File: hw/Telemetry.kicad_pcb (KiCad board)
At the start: 4 copper layers, 100 x 82 mm, 132 parts, among them J102 BOOT0, J103 SPORT, J104 SBUS, J105 USB_B_Micro, J106 UART_EXP, J201 Conn_01x02, J301 Conn_01x02, J302 Conn_01x02, J401 Conn_01x02, J402 Conn_01x02, J403 Conn_01x02, J404 Conn_01x02, J405 Conn_01x02, J406 Conn_01x02, J407 Conn_01x02, J408 Conn_01x02, J409 ServoCon, J410 AUDIO, Q401 IRLML6344TRPBF, Q402 IRLML6344TRPBF, Q403 IRLML6344TRPBF, Q404 CSD17306Q5A, Q406 IRLML6344TRPBF, Q408 CSD17306Q5A, SW101 SW_Push, U101 STM32F303CBx, U102 IS25LP032D, U201 AP1501-K5, U202 RT6200, U301 LP2985-5.0, U302 ACS770xCB-100U-PSF, U303 MCP6001-OT, U304 ACS770xCB-100U-PSF, U305 MCP6001-OT, U401 MCP1416, U402 MCP1416, U403 AD5160BRJZ10-R2, U404 MCP6001-OT, U405 TLP2361_TPL_E, U406 TLP2361_TPL_E, X101 SG-310_SCF_8.000000MHZ

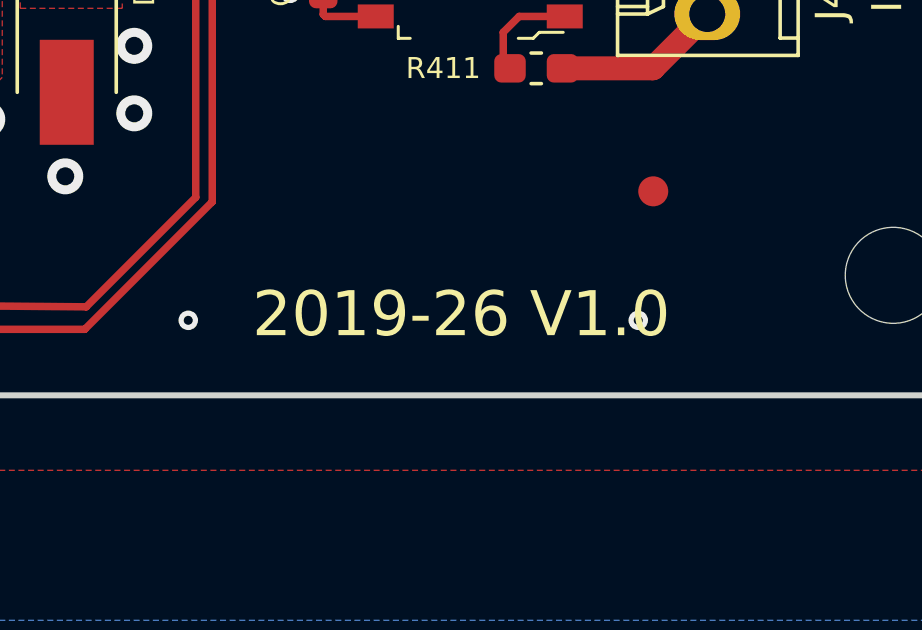
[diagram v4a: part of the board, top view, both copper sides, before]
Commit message: Added board 3D model picture to readme
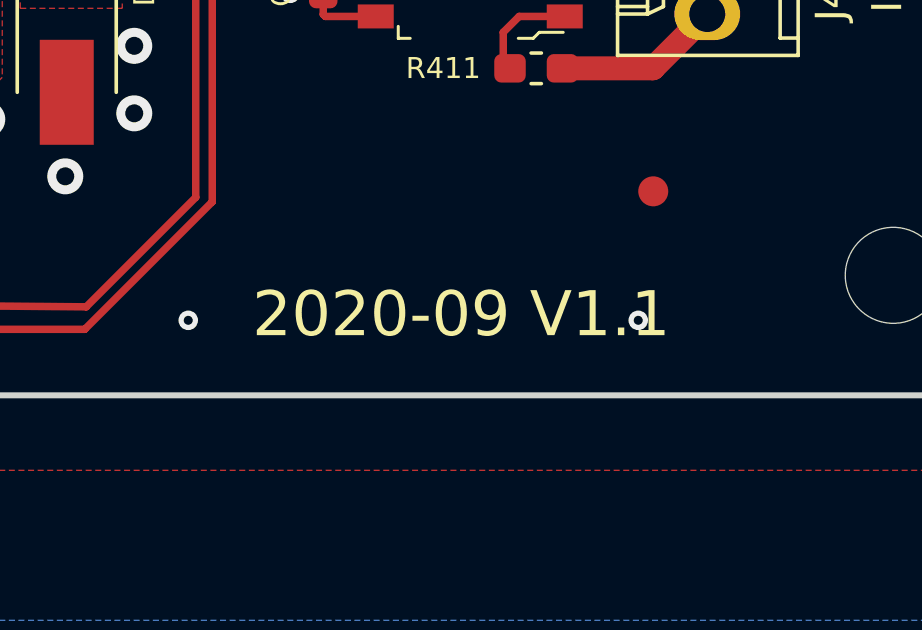
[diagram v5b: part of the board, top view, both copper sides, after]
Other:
- board text added: "2020-09 V1.1"
- board text removed: "2019-26 V1.0"
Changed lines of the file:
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@@
     (pad 1 smd rect (at -5.25 0) (size 4.5 5) (layers F.Cu F.Paste F.Mask)
       (net 9 "Net-(D202-Pad1)"))
+    (model ${KISYS3DMOD}/Inductor_SMD.3dshapes/L_Bourns_SRR1260.step
+      (at (xyz 0 0 0))
+      (scale (xyz 1 1 1))
+      (rotate (xyz 0 0 0))
+    )
   )
   (module digikey-footprints:SOT-23-3 (layer F.Cu)
@@
     (pad 6 smd rect (at -1.27 -3.15 90) (size 0.8 1.2) (layers F.Cu F.Paste F.Mask)
       (net 2 +3V3))
+    (model ${KISYS3DMOD}/Package_SO.3dshapes/SO-6_4.4x3.6mm_P1.27mm.step
+      (at (xyz 0 0 0))
+      (scale (xyz 1 1 1))
+      (rotate (xyz 0 0 -90))
+    )
   )
   (module digikey-footprints:SOIC-6-5_W4.55mm (layer F.Cu)
@@
     (pad 1 smd rect (at -1.27 3.15 90) (size 0.8 1.2) (layers F.Cu F.Paste F.Mask)
       (net 63 "Net-(R411-Pad1)"))
+    (model ${KISYS3DMOD}/Package_SO.3dshapes/SO-6_4.4x3.6mm_P1.27mm.step
+      (at (xyz 0 0 0))
+      (scale (xyz 1 1 1))
+      (rotate (xyz 0 0 -90))
+    )
   )
   (module Pin_Headers:Pin_Header_Straight_2x03 (layer F.Cu)
@@
     (pad 6 thru_hole oval (at 2.54 5.08) (size 1.7272 1.7272) (drill 1.016) (layers *.Cu *.Mask F.SilkS)
       (net 1 GND))
-    (model Pin_Headers.3dshapes/Pin_Header_Straight_2x03.wrl
-      (offset (xyz 1.269999980926514 -2.539999961853027 0))
+    (model ${KISYS3DMOD}/Connector_PinHeader_2.54mm.3dshapes/PinHeader_2x03_P2.54mm_Vertical.step
+      (at (xyz 0 0 0))
       (scale (xyz 1 1 1))
-      (rotate (xyz 0 0 90))
+      (rotate (xyz 0 0 0))
     )
   )
@@
     (pad 1 thru_hole rect (at 0 0 90) (size 1.7272 1.7272) (drill 1.016) (layers *.Cu *.Mask F.SilkS)
       (net 17 /Sbus))
-    (model Pin_Headers.3dshapes/Pin_Header_Straight_2x03.wrl
+    (model ${KISYS3DMOD}/Connector_PinHeader_2.54mm.3dshapes/PinHeader_2x03_P2.54mm_Vertical.step
       (offset (xyz 1.269999980926514 -2.539999961853027 0))
       (scale (xyz 1 1 1))
@@
     (pad 6 thru_hole oval (at 2.54 5.08 90) (size 1.7 1.7) (drill 1) (layers *.Cu *.Mask)
       (net 1 GND))
-    (model ${KISYS3DMOD}/Connector_PinHeader_2.54mm.3dshapes/PinHeader_2x03_P2.54mm_Vertical.wrl
+    (model ${KISYS3DMOD}/Connector_PinHeader_2.54mm.3dshapes/PinHeader_2x03_P2.54mm_Vertical.step
       (at (xyz 0 0 0))
       (scale (xyz 1 1 1))
@@
     (pad 4 thru_hole oval (at 2.54 2.54 90) (size 1.7 1.7) (drill 1) (layers *.Cu *.Mask)
       (net 1 GND))
-    (model ${KISYS3DMOD}/Connector_PinHeader_2.54mm.3dshapes/PinHeader_2x02_P2.54mm_Vertical.wrl
+    (model ${KISYS3DMOD}/Connector_PinHeader_2.54mm.3dshapes/PinHeader_2x02_P2.54mm_Vertical.step
       (at (xyz 0 0 0))
       (scale (xyz 1 1 1))
@@
     (pad 2 smd rect (at 1.85 0 90) (size 1.5 2.5) (layers F.Cu F.Paste F.Mask)
       (net 2 +3V3))
+    (model ${KISYS3DMOD}/Inductor_SMD.3dshapes/L_Bourns-SRN4018.step
+      (at (xyz 0 0 0))
+      (scale (xyz 1.2 1 1))
+      (rotate (xyz 0 0 0))
+    )
   )
   (gr_text S.port (at 157.8 64.9 90) (layer F.SilkS)
@@
   (gr_poly (pts (xy 70.6 62.5) (xy 91.1 62.5) (xy 91.1 64.3) (xy 70.6 64.3)) (layer F.Mask) (width 0.15))
   (gr_poly (pts (xy 70.7 58.3) (xy 81.5 58.3) (xy 82.6 58.3) (xy 85.1 60.8) (xy 91 60.8) (xy 91 61.8) (xy 84.5 61.8) (xy 70.7 61.8)) (layer F.Mask) (width 0.15))
-  (gr_text "2019-26 V1.0" (at 141.6 117.3) (layer F.SilkS)
+  (gr_text "2020-09 V1.1" (at 141.6 117.3) (layer F.SilkS)
     (effects (font (size 1.5 1.5) (thickness 0.3)))
   )

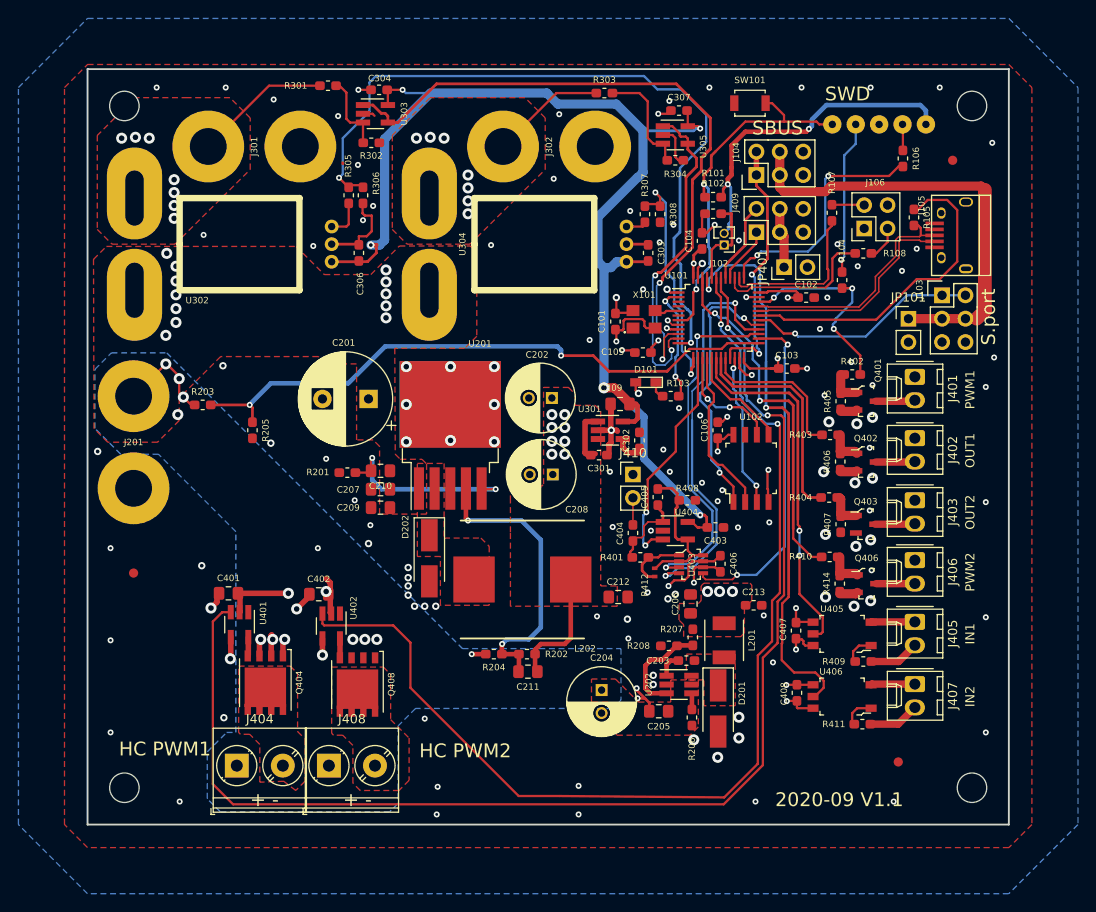
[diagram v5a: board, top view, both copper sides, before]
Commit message: BOM Generation for 1.1 version
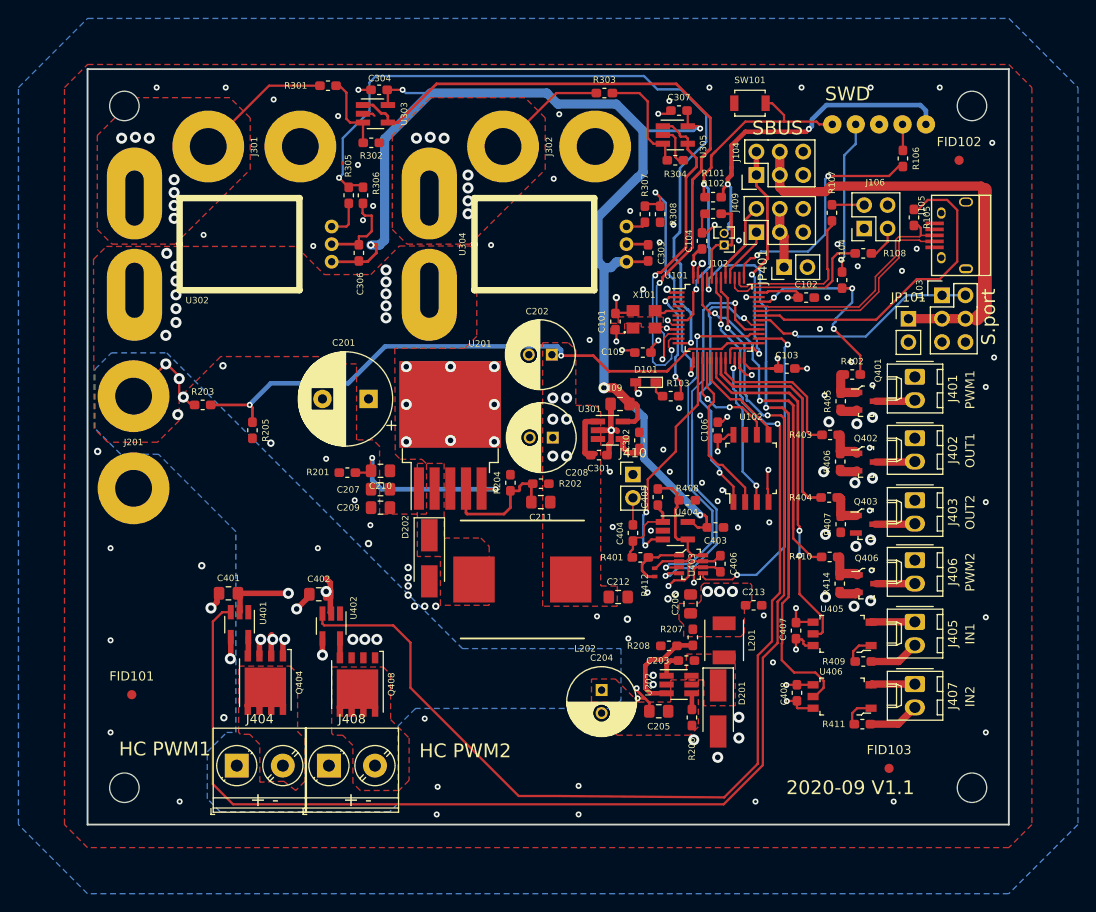
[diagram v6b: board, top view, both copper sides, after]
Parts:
- removed REF** (x3): Fiducial_1mm_Dia_2.54mm_Outer_CopperTop, Fiducials:Fiducial_1mm_Dia_2.54mm_Outer_CopperTop
- added FID101: Fiducial, Fiducial:Fiducial_1mm_Mask2mm, F.Cu at (64.8, 105.9)
- added FID102: Fiducial, Fiducial:Fiducial_1mm_Mask2mm, F.Cu at (154.6, 47.9)
- added FID103: Fiducial, Fiducial:Fiducial_1mm_Mask2mm, F.Cu at (147.0, 113.9)
- C101, C102, C103, C104, C105, C106, C207, C211, C212, C303, C304, C306, C307, C403, C405, C406, C407, C408: value 100n -> 100n/50V
- C203: value 100n -> 10n/50V
- C204: value 22u -> 22u/35V
- C205, C301, C401, C402: value 1u -> 1u/35V
- C206, C404: value 10u -> 10u/10V
- C209, C210, C213, C302: value 10n -> 10n/50V
- C309: value 2u2 -> 2u2/10V
- D101: value LED -> LED_Green
- moved R204 18.7 mm to (105.9, 82.9), turned to 90 degrees
- moved R202 18.6 mm to (109.2, 83.0)
- moved C211 18.5 mm to (109.2, 85.0)
- moved C202 4.70 mm to (110.4, 69.0)
- moved C208 4.00 mm to (110.5, 78.0)
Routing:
- net Net-(C211-Pad2): track 31.7 -> 14.7 mm, vias 2 -> 0
- net VCC: track 26.9 -> 13.7 mm, vias 9 -> 7
- net GND: track 91.5 -> 84.0 mm, vias 146 -> 145

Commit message: DAC Amplifier improvements
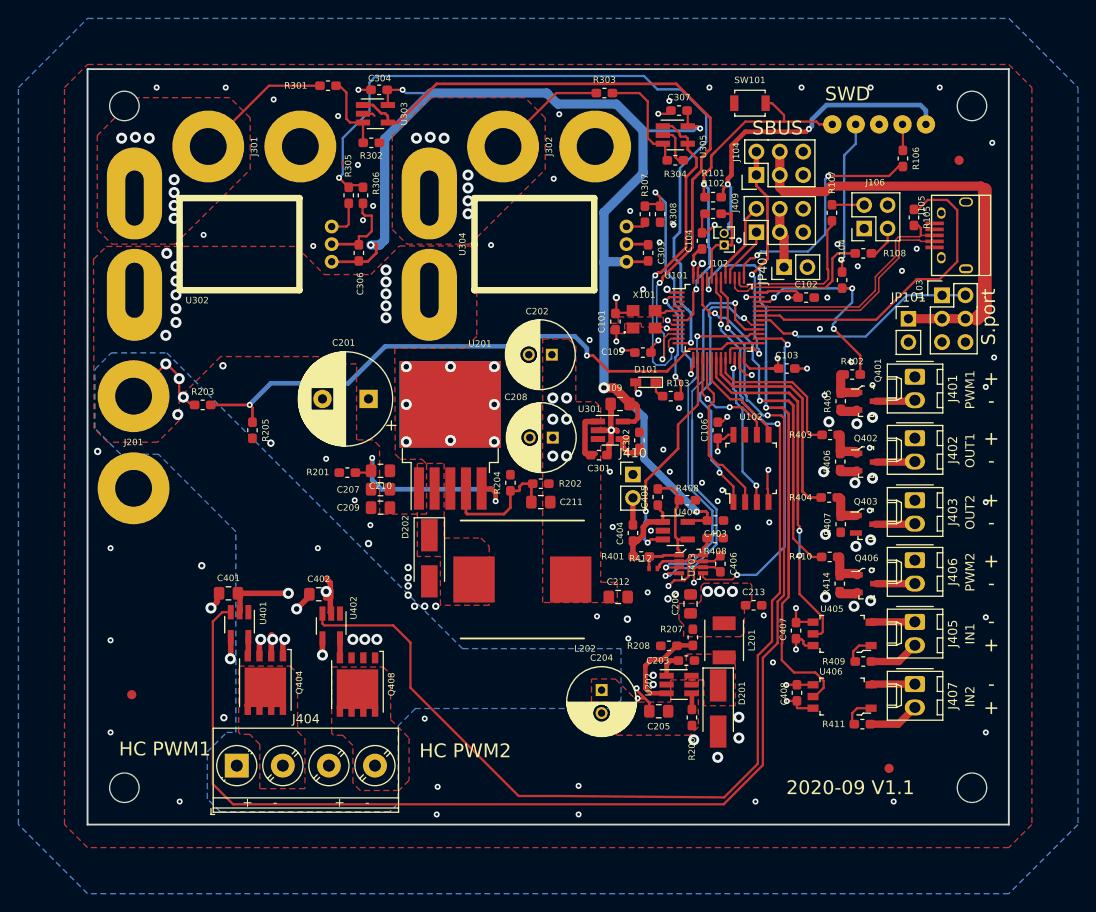
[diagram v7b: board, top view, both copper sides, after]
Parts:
- removed J408: Conn_01x02, TerminalBlock_Phoenix:TerminalBlock_Phoenix_PT-1,5-2-5.0-H_1x02_P5.00mm_Horizontal
- added R408: 1k, Resistor_SMD:R_0603_1608Metric_Pad1.05x0.95mm_HandSolder, F.Cu at (128.1, 88.9)
- J404: value Conn_01x02 -> HC_OUT; footprint TerminalBlock_Phoenix:TerminalBlock_Phoenix_PT-1,5-2-5.0-H_1x02_P5.00mm_Horizontal -> TerminalBlock_Phoenix:TerminalBlock_Phoenix_PT-1,5-4-5.0-H_1x04_P5.00mm_Horizontal
- U302, U304: value ACS770xCB-100U-PSF -> ACS758LCB-100B-PFF-T
- moved C403 0.75 mm to (128.2, 87.0)
- moved R412 0.46 mm to (121.4, 92.2), turned to 0 degrees
- moved R401 0.14 mm to (120.1, 90.9)
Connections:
- Q408 pad 5: Net-(J408-Pad2) -> Net-(J404-Pad4)
- R401 pad 2: Net-(R401-Pad2) -> Net-(C405-Pad2)
- R412 pad 1: Net-(R401-Pad2) -> Net-(C405-Pad2)
- R412 pad 2: Net-(C405-Pad2) -> Net-(R408-Pad2)
- U403 pad 1: Net-(C405-Pad2) -> Net-(R408-Pad2)
- U403 pad 7: Net-(C405-Pad2) -> Net-(R408-Pad2)
- U403 pad 8: Net-(R401-Pad2) -> Net-(C405-Pad2)
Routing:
- net Net-(R408-Pad2): track 0.00 -> 7.73 mm
- net Net-(R401-Pad2): track 6.74 -> 0.00 mm
- net Net-(C404-Pad2): track 8.34 -> 13.6 mm
- net Net-(C210-Pad2): track 21.0 -> 23.2 mm
- net Net-(C405-Pad2): track 16.4 -> 15.0 mm
- net +5VA: track 132.8 -> 131.4 mm
- net BAT_VOLTAGE: track 66.4 -> 67.4 mm
- net DAC_OUT: track 25.1 -> 24.4 mm
- net Net-(C404-Pad1): track 2.41 -> 2.93 mm
- added copper zone on F.Cu, net Net-(J404-Pad4)
- removed copper zone on F.Cu, net Net-(J408-Pad2)

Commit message: Added additional opamp to DAC output as a buffer.
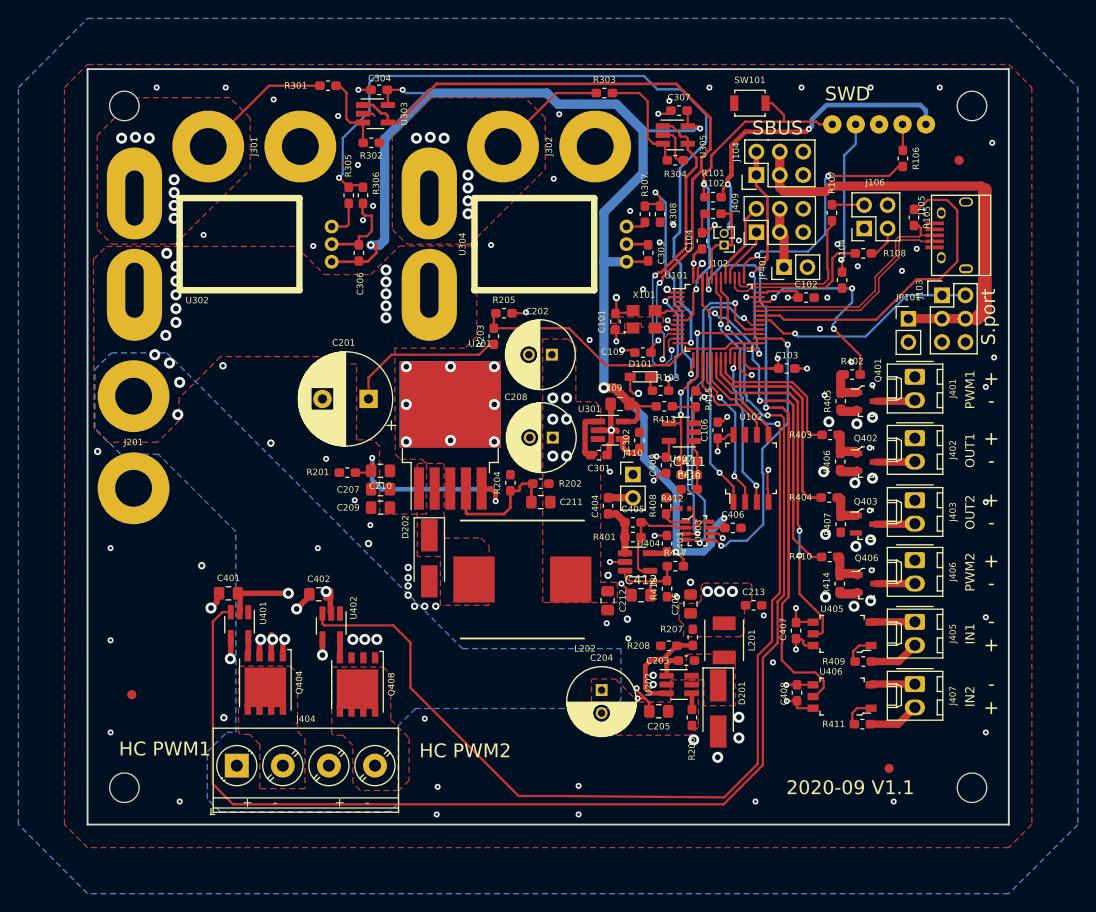
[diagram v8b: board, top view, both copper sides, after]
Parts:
- removed the R408 at (125.1, 84.8)
- added C409: 100n/50V, Capacitor_SMD:C_0603_1608Metric_Pad1.05x0.95mm_HandSolder, F.Cu at (122.8, 81.0)
- added C410: 10u/10V, Capacitor_SMD:C_0603_1608Metric_Pad1.05x0.95mm_HandSolder, F.Cu at (125.3, 83.6)
- added C411: 100n/50V, Capacitor_SMD:C_0603_1608Metric_Pad1.05x0.95mm_HandSolder, F.Cu at (125.3, 82.0)
- added C412: 100n/50V, Capacitor_SMD:C_0805_2012Metric_Pad1.15x1.40mm_HandSolder, F.Cu at (120.1, 95.1)
- added R413: 10k, Resistor_SMD:R_0603_1608Metric_Pad1.05x0.95mm_HandSolder, F.Cu at (122.6, 74.6)
- added R415: 10k, Resistor_SMD:R_0603_1608Metric_Pad1.05x0.95mm_HandSolder, F.Cu at (126.0, 73.8)
- added R416: 15k, Resistor_SMD:R_0603_1608Metric_Pad1.05x0.95mm_HandSolder, F.Cu at (125.3, 80.5)
- added R417: 10k, Resistor_SMD:R_0603_1608Metric_Pad1.05x0.95mm_HandSolder, F.Cu at (123.8, 92.0)
- added R418: 10k, Resistor_SMD:R_0603_1608Metric_Pad1.05x0.95mm_HandSolder, F.Cu at (122.9, 94.4)
- added U407: MCP6001-OT, Package_TO_SOT_SMD:SOT-23-5_HandSoldering, F.Cu at (124.5, 77.4)
- R408: value 1k -> 3k3
- U202: footprint TO_SOT_Packages_SMD:SOT-23-6_Handsoldering -> Package_TO_SOT_SMD:SOT-23-6_Handsoldering
- U301, U305, U401, U402, U404: footprint TO_SOT_Packages_SMD:SOT-23-5_HandSoldering -> Package_TO_SOT_SMD:SOT-23-5_HandSoldering
- moved R203 32.5 mm to (104.1, 67.0), turned to 90 degrees
- moved R205 30.1 mm to (105.2, 64.5), turned to 0 degrees
- moved R412 7.36 mm to (124.8, 85.7)
- moved R408 6.37 mm to (122.8, 85.4), turned to 90 degrees
- moved C403 5.81 mm to (122.9, 89.5), turned to 270 degrees
- moved U404 5.33 mm to (119.7, 91.5)
- moved C406 4.12 mm to (130.1, 87.8), turned to 0 degrees
- moved C404 4.00 mm to (116.5, 85.4)
- moved C405 3.85 mm to (119.2, 87.2), turned to 0 degrees
- moved U403 3.71 mm to (126.2, 88.1)
- moved R401 2.28 mm to (119.2, 88.8)
- moved R103 1.25 mm to (122.2, 72.9)
- moved C212 1.22 mm to (116.5, 95.7), turned to 270 degrees
- moved D101 0.85 mm to (120.0, 71.4)
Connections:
- C406 pad 1: VCC -> +5VA
- R408 pad 1: GND -> Net-(R408-Pad1)
- R408 pad 2: Net-(R408-Pad2) -> Net-(C410-Pad1)
- R412 pad 1: Net-(C405-Pad2) -> Net-(R408-Pad1)
- R412 pad 2: Net-(R408-Pad2) -> Net-(C405-Pad2)
- U403 pad 1: Net-(R408-Pad2) -> Net-(C405-Pad2)
- U403 pad 2: VCC -> +5VA
- U403 pad 7: Net-(R408-Pad2) -> Net-(C405-Pad2)
- U403 pad 8: Net-(C405-Pad2) -> Net-(R408-Pad1)
- U404 pad 3: DAC_OUT -> Net-(C412-Pad2)
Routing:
- net BAT_VOLTAGE: track 67.4 -> 33.1 mm, vias 2 -> 0
- net +5VA: track 131.4 -> 152.4 mm, vias 5 -> 7
- net DAC_OUT: track 24.4 -> 14.8 mm
- net Net-(C412-Pad2): track 0.00 -> 8.49 mm
- net Net-(C404-Pad2): track 13.6 -> 5.57 mm
- net VCC: track 13.7 -> 5.91 mm, vias 7 -> 6
- net Net-(R408-Pad2): track 7.73 -> 0.00 mm
- net AMP_CS: track 38.3 -> 30.8 mm
- net GND: track 84.0 -> 91.3 mm, vias 145 -> 140
- net AMP_DIN: track 44.2 -> 36.9 mm
- net Net-(C410-Pad2): track 0.00 -> 5.41 mm
- net AMP_CLK: track 36.3 -> 31.2 mm
- net +BATT: track 22.1 -> 26.9 mm
- net Net-(R413-Pad1): track 0.00 -> 4.41 mm
- net Net-(R408-Pad1): track 0.00 -> 4.40 mm
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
